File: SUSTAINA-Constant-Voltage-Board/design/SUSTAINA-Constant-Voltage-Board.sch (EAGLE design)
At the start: 25 parts, among them M1 I7C4W012A050V-0C1-R, M2 POWER-MONITOR-MODULE, M3 USB-TO-QUAD-RS-485-CONV-MODUL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

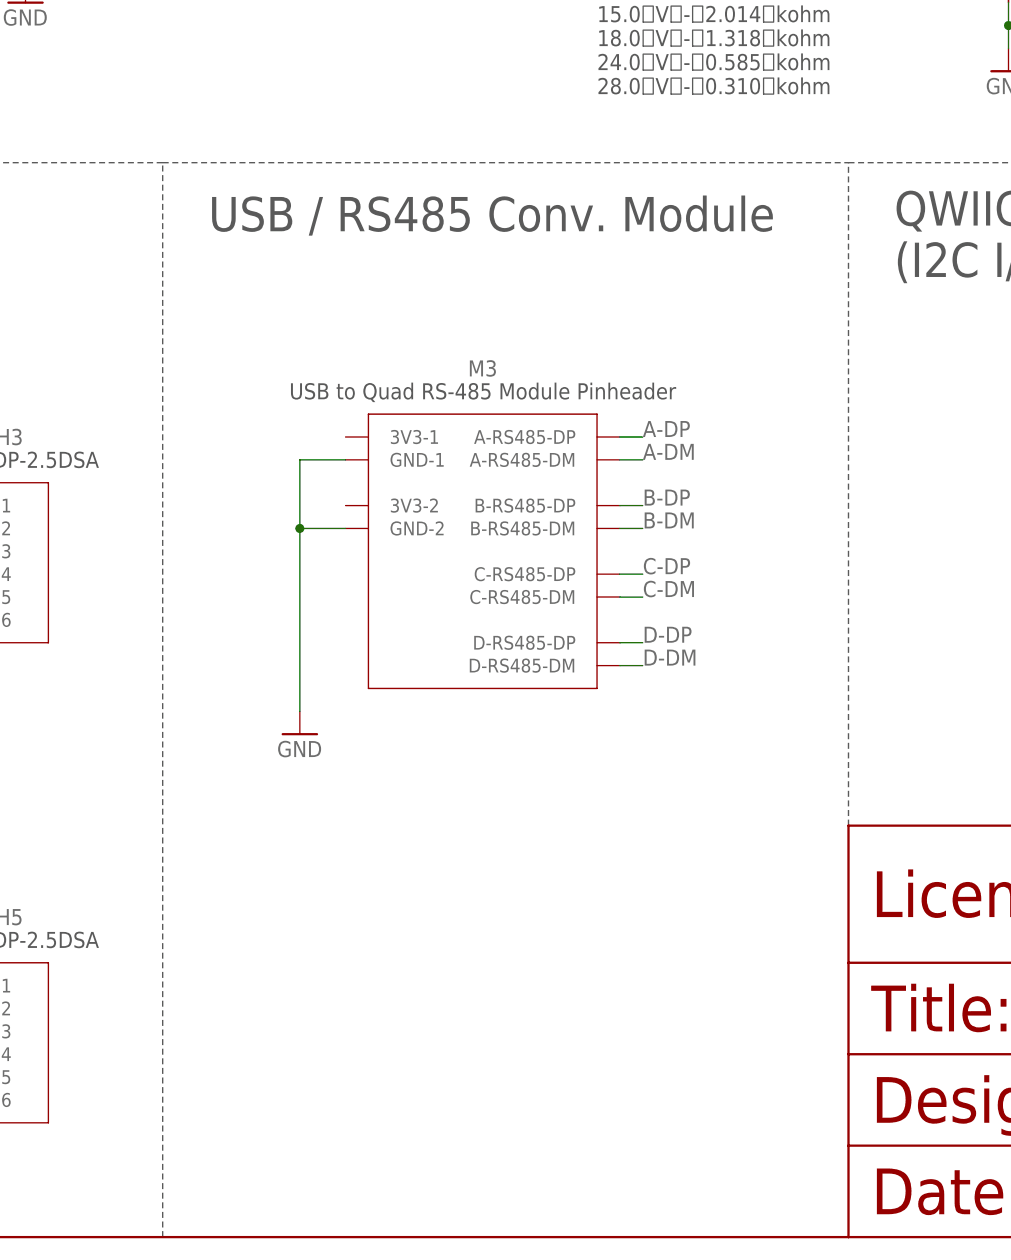
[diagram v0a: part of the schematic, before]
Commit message: Added connector for DC fans to SUSTAINA-Constant-Voltage-Board
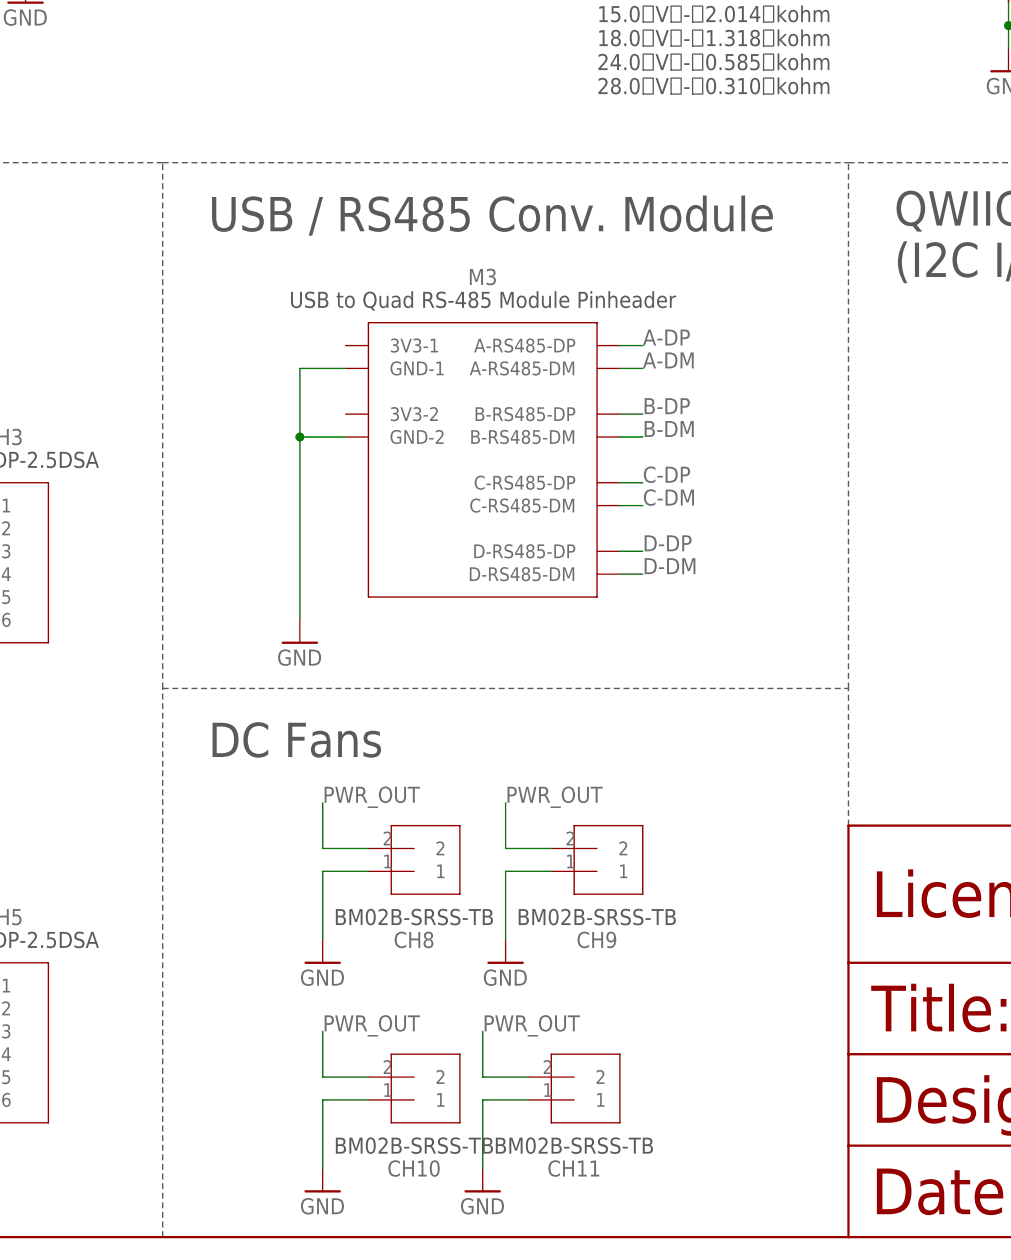
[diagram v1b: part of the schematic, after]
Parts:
- added CH10, CH11, CH8, CH9: BM02B-SRSS-TB, SH-Connecters:BM02B-SRSS-TB
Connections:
- net GND: now also CH10.1, CH11.1, CH8.1, CH9.1
- net PWR_OUT: now also CH10.2, CH11.2, CH8.2, CH9.2
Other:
- note added: "DC Fans"
- moved on the sheet: M3

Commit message: Revert Constant-Voltage-Board to version without fan connectors and add data and documentation for outsourcing
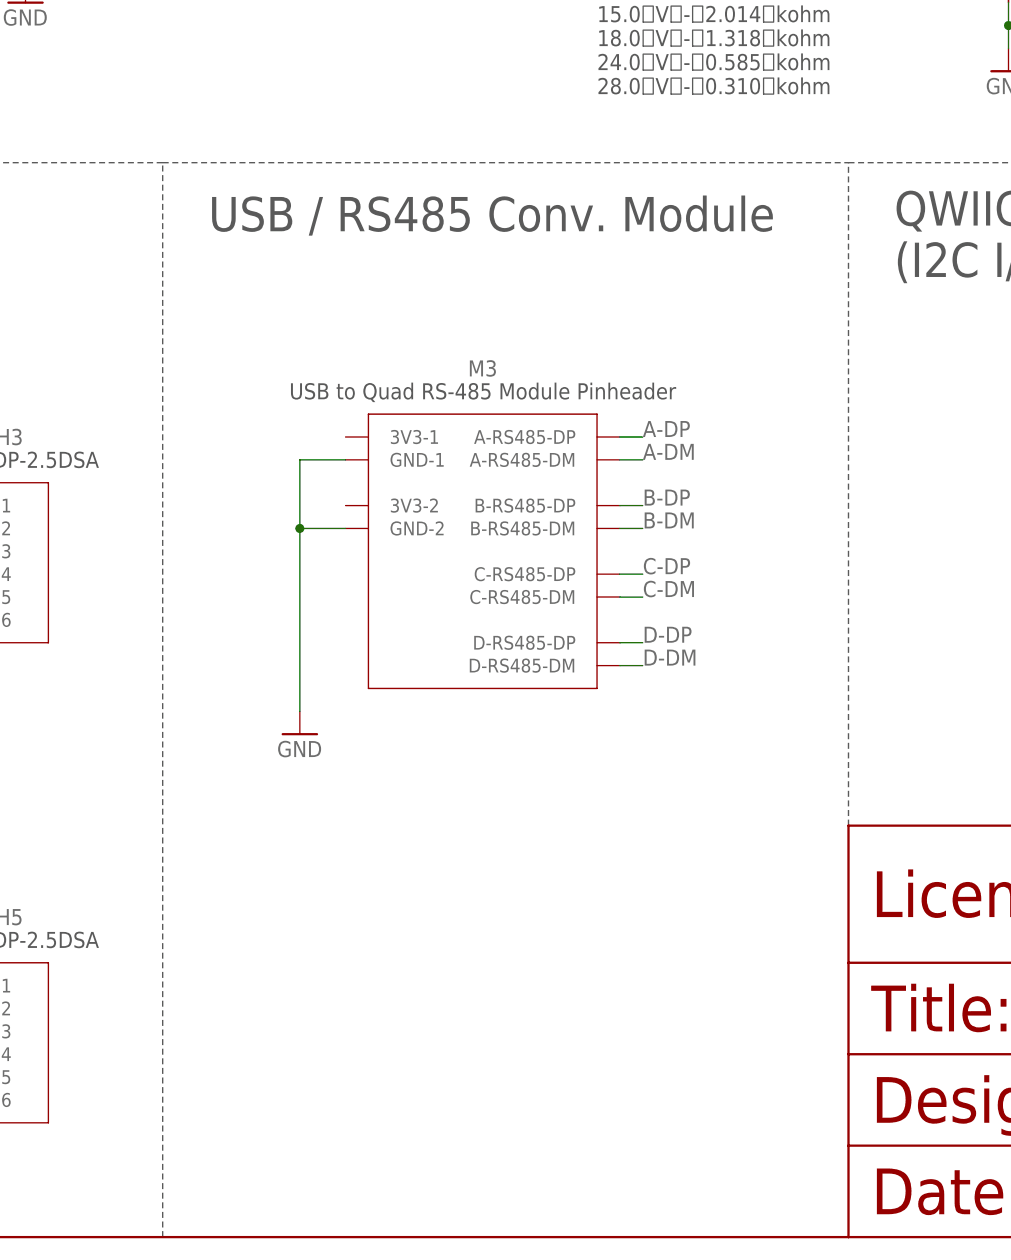
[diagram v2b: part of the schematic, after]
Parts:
- removed CH10, CH11, CH8, CH9: BM02B-SRSS-TB, SH-Connecters:BM02B-SRSS-TB
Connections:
- net GND: no longer CH10.1, CH11.1, CH8.1, CH9.1
- net PWR_OUT: no longer CH10.2, CH11.2, CH8.2, CH9.2
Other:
- note removed: "DC Fans"
- moved on the sheet: M3
